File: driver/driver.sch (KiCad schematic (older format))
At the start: 107 parts, among them J1 OUT_A, J2 OUT_B, J3 UART_DEBUG, J4 USB_B_Micro, J5 CH340E module, J6 1602 I2C LCD, J7 IN_VCC, J8 IN_GND, Q1 TPHR6503PL, Q2 TPHR6503PL, Q3 TPHR6503PL, Q4 TPHR6503PL, SW1 SW_Push, SW2 SW_Push, U1 MT3608, U10 PC817, U2 AMS1117-5.0, U3 AMS1117-3.3, U4 TC4427, U5 TC4427, U6 STM32F103C8Tx, U7 INA226, U8 MCP9804_MSOP, U9 PC817, Y1 8MHz

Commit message: driver: Continue layout
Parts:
- removed C6: 100u, Capacitor_THT:CP_Radial_D12.5mm_P5.00mm, symbol Device:CP_Small
- removed C7, C8: 1u, Capacitors_SMD:C_0603_HandSoldering, symbol Device:C_Small
- removed R6: 10R .5W, Resistor_SMD:R_1206_3216Metric_Pad1.42x1.75mm_HandSolder, symbol Device:R_Small
- added C6: 100n, Capacitors_SMD:C_0603_HandSoldering, symbol Device:C_Small
- C15: footprint Capacitors_SMD:C_0603_HandSoldering -> Capacitor_THT:CP_Radial_D10.0mm_P5.00mm
- C19, C2, C3: footprint Capacitor_THT:CP_Radial_D12.5mm_P5.00mm -> Capacitor_THT:CP_Radial_D10.0mm_P5.00mm
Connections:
- net +3V3: now also C6.1
- net GND: now also C6.2; no longer U8.4 (GND), U8.5 (A2), U8.6 (A1), U8.7 (A0)
- net GND_MEAS: now also U8.4 (GND), U8.5 (A2), U8.6 (A1), U8.7 (A0)
- net LED2: now also U6.15 (PA5); no longer U6.20 (PB2)
- net LED5: now also U6.16 (PA6); no longer U6.15 (PA5)
- net LED6: now also U6.20 (PB2); no longer U6.16 (PA6)
- net at C15.1, C16.1, R7.2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: now also U2.3 (VI)
- net at D4.2 (A): now also R16.2; no longer R13.2
- net at D7.2 (A): now also R13.2; no longer R16.2
- net at D8.2 (A): now also R18.2; no longer R17.2
- net at D9.2 (A): now also R17.2; no longer R18.2
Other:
- moved on the sheet: C29, D4, D7, D8, D9
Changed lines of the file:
@@
 F 0 "C15" H 13000 4300 50  0000 L CNN
 F 1 "100u" H 13000 4200 50  0000 L CNN
-F 2 "Capacitors_SMD:C_0603_HandSoldering" H 13250 4250 50  0001 C CNN
+F 2 "Capacitor_THT:CP_Radial_D10.0mm_P5.00mm" H 13250 4250 50  0001 C CNN
 F 3 "~" H 13250 4250 50  0001 C CNN
 	1    13250 4250
@@
 $EndComp
 Wire Wire Line
-	12950 4100 13250 4100
-Wire Wire Line
 	13250 4100 13250 4150
 Wire Wire Line
@@
 F 0 "C19" H 15200 4300 50  0000 L CNN
 F 1 "470u" H 15200 4200 50  0000 L CNN
-F 2 "Capacitor_THT:CP_Radial_D12.5mm_P5.00mm" H 15100 4250 50  0001 C CNN
+F 2 "Capacitor_THT:CP_Radial_D10.0mm_P5.00mm" H 15100 4250 50  0001 C CNN
 F 3 "~" H 15100 4250 50  0001 C CNN
 	1    15100 4250
@@
 	13600 2200 13600 2050
 Connection ~ 13600 2050
-Wire Wire Line
-	12650 2050 12650 3200
 Connection ~ 12650 4100
 Wire Wire Line
@@
 F 0 "C2" H 15700 2150 50  0000 L CNN
 F 1 "470u" H 15700 2050 50  0000 L CNN
-F 2 "Capacitor_THT:CP_Radial_D12.5mm_P5.00mm" H 15600 2100 50  0001 C CNN
+F 2 "Capacitor_THT:CP_Radial_D10.0mm_P5.00mm" H 15600 2100 50  0001 C CNN
 F 3 "~" H 15600 2100 50  0001 C CNN
 	1    15600 2100
@@
 F 0 "C3" H 12850 2300 50  0000 L CNN
 F 1 "470u" H 12850 2200 50  0000 L CNN
-F 2 "Capacitor_THT:CP_Radial_D12.5mm_P5.00mm" H 13100 2250 50  0001 C CNN
+F 2 "Capacitor_THT:CP_Radial_D10.0mm_P5.00mm" H 13100 2250 50  0001 C CNN
 F 3 "~" H 13100 2250 50  0001 C CNN
 	1    13100 2250
@@
 L Device:C_Small C29
 U 1 1 5C5F270F
-P 11600 7750
-F 0 "C29" H 11692 7796 50  0000 L CNN
-F 1 "100n" H 11700 7700 50  0000 L CNN
-F 2 "Capacitors_SMD:C_0603_HandSoldering" H 11600 7750 50  0001 C CNN
-F 3 "~" H 11600 7750 50  0001 C CNN
-	1    11600 7750
+P 11450 7750
+F 0 "C29" H 11542 7796 50  0000 L CNN
+F 1 "100n" H 11550 7700 50  0000 L CNN
+F 2 "Capacitors_SMD:C_0603_HandSoldering" H 11450 7750 50  0001 C CNN
+F 3 "~" H 11450 7750 50  0001 C CNN
+	1    11450 7750
 	1    0    0    -1
 $EndComp
@@
 L power:GND #PWR0119
 U 1 1 5C5F5707
-P 11600 7850
-F 0 "#PWR0119" H 11600 7600 50  0001 C CNN
-F 1 "GND" H 11605 7677 50  0000 C CNN
-F 2 "" H 11600 7850 50  0001 C CNN
-F 3 "" H 11600 7850 50  0001 C CNN
-	1    11600 7850
+P 11450 7850
+F 0 "#PWR0119" H 11450 7600 50  0001 C CNN
+F 1 "GND" H 11455 7677 50  0000 C CNN
+F 2 "" H 11450 7850 50  0001 C CNN
+F 3 "" H 11450 7850 50  0001 C CNN
+	1    11450 7850
 	1    0    0    -1
 $EndComp
@@
 L power:+3V3 #PWR0128
 U 1 1 5C7621FB
-P 11600 7650
-F 0 "#PWR0128" H 11600 7500 50  0001 C CNN
-F 1 "+3V3" H 11615 7823 50  0000 C CNN
-F 2 "" H 11600 7650 50  0001 C CNN
-F 3 "" H 11600 7650 50  0001 C CNN
-	1    11600 7650
+P 11450 7650
+F 0 "#PWR0128" H 11450 7500 50  0001 C CNN
+F 1 "+3V3" H 11465 7823 50  0000 C CNN
+F 2 "" H 11450 7650 50  0001 C CNN
+F 3 "" H 11450 7650 50  0001 C CNN
+	1    11450 7650
 	1    0    0    -1
 $EndComp
@@
 $EndComp
 $Comp
-L Device:C_Small C8
-U 1 1 5D0CB164
-P 14400 3350
-F 0 "C8" H 14492 3396 50  0000 L CNN
-F 1 "1u" H 14500 3300 50  0000 L CNN
-F 2 "Capacitors_SMD:C_0603_HandSoldering" H 14400 3350 50  0001 C CNN
-F 3 "~" H 14400 3350 50  0001 C CNN
-	1    14400 3350
-	1    0    0    -1
-$EndComp
-Wire Wire Line
-	14400 3450 14400 3500
-Wire Wire Line
-	14400 3250 14400 3200
-Wire Wire Line
-	14400 3200 14300 3200
-$Comp
-L Device:C_Small C7
-U 1 1 5D0CB16E
-P 13600 3350
-F 0 "C7" H 13400 3400 50  0000 L CNN
-F 1 "1u" H 13400 3300 50  0000 L CNN
-F 2 "Capacitors_SMD:C_0603_HandSoldering" H 13600 3350 50  0001 C CNN
-F 3 "~" H 13600 3350 50  0001 C CNN
-	1    13600 3350
-	1    0    0    -1
-$EndComp
-Wire Wire Line
-	13600 3500 13600 3450
-Wire Wire Line
-	13600 3250 13600 3200
-Wire Wire Line
-	13600 3200 13700 3200
-$Comp
-L Device:CP_Small C6
-U 1 1 5D0CB178
-P 13250 3350
-F 0 "C6" H 13000 3400 50  0000 L CNN
-F 1 "100u" H 13000 3300 50  0000 L CNN
-F 2 "Capacitor_THT:CP_Radial_D12.5mm_P5.00mm" H 13250 3350 50  0001 C CNN
-F 3 "~" H 13250 3350 50  0001 C CNN
-	1    13250 3350
-	1    0    0    -1
-$EndComp
-$Comp
-L Device:R_Small R6
-U 1 1 5D0CB17F
-P 12850 3200
-F 0 "R6" V 12654 3200 50  0000 C CNN
-F 1 "10R .5W" V 12745 3200 50  0000 C CNN
-F 2 "Resistor_SMD:R_1206_3216Metric_Pad1.42x1.75mm_HandSolder" H 12850 3200 50  0001 C CNN
-F 3 "~" H 12850 3200 50  0001 C CNN
-	1    12850 3200
-	0    -1   1    0
-$EndComp
-Wire Wire Line
-	12950 3200 13250 3200
-Wire Wire Line
-	13250 3200 13250 3250
-Wire Wire Line
-	13250 3200 13600 3200
-Connection ~ 13250 3200
-Connection ~ 13600 3200
-$Comp
 L power:GND #PWR0140
 U 1 1 5D0CB18B
@@
 	1    0    0    -1
 $EndComp
-Wire Wire Line
-	14400 3500 14000 3500
-Wire Wire Line
-	13250 3500 13250 3450
-Connection ~ 13600 3500
-Wire Wire Line
-	13600 3500 13250 3500
 Connection ~ 14000 3500
-Wire Wire Line
-	14000 3500 13600 3500
 Wire Wire Line
 	14000 3500 14000 3550
@@
 	14750 3250 14750 3200
 Wire Wire Line
-	14750 3200 14400 3200
-Connection ~ 14400 3200
-Wire Wire Line
-	14400 3500 14750 3500
-Wire Wire Line
 	14750 3500 14750 3450
-Connection ~ 14400 3500
 $Comp
 L Device:C_Small C9
@@
 Wire Wire Line
 	15100 3100 15100 3200
-Wire Wire Line
-	12750 3200 12650 3200
-Connection ~ 12650 3200
-Wire Wire Line
-	12650 3200 12650 4100
 $Comp
 L Device:LED_Small_ALT D2
@@
 L Device:LED_Small_ALT D4
 U 1 1 5D120495
-P 18100 5600
-F 0 "D4" V 18200 5550 50  0000 R CNN
-F 1 "cyan" V 18055 5532 50  0001 R CNN
-F 2 "LED_SMD:LED_PLCC_2835_Handsoldering" V 18100 5600 50  0001 C CNN
-F 3 "~" V 18100 5600 50  0001 C CNN
-	1    18100 5600
+P 18800 5600
+F 0 "D4" V 18900 5550 50  0000 R CNN
+F 1 "cyan" V 18755 5532 50  0001 R CNN
+F 2 "LED_SMD:LED_PLCC_2835_Handsoldering" V 18800 5600 50  0001 C CNN
+F 3 "~" V 18800 5600 50  0001 C CNN
+	1    18800 5600
 	0    -1   -1   0
 $EndComp
@@
 L Device:LED_Small_ALT D7
 U 1 1 5D12562A
-P 18800 5600
-F 0 "D7" V 18900 5550 50  0000 R CNN
-F 1 "pink" V 18755 5532 50  0001 R CNN
-F 2 "LED_SMD:LED_PLCC_2835_Handsoldering" V 18800 5600 50  0001 C CNN
-F 3 "~" V 18800 5600 50  0001 C CNN
-	1    18800 5600
+P 18100 5600
+F 0 "D7" V 18200 5550 50  0000 R CNN
+F 1 "pink" V 18055 5532 50  0001 R CNN
+F 2 "LED_SMD:LED_PLCC_2835_Handsoldering" V 18100 5600 50  0001 C CNN
+F 3 "~" V 18100 5600 50  0001 C CNN
+	1    18100 5600
 	0    -1   -1   0
 $EndComp
@@
 L Device:LED_Small_ALT D8
 U 1 1 5D1365C9
+P 19200 5600
+F 0 "D8" V 19300 5550 50  0000 R CNN
+F 1 "pink" V 19155 5532 50  0001 R CNN
+F 2 "LED_SMD:LED_PLCC_2835_Handsoldering" V 19200 5600 50  0001 C CNN
+F 3 "~" V 19200 5600 50  0001 C CNN
+	1    19200 5600
+	0    -1   -1   0
+$EndComp
+$Comp
+L Device:LED_Small_ALT D9
+U 1 1 5D138D62
 P 19000 5600
-F 0 "D8" V 19100 5550 50  0000 R CNN
+F 0 "D9" V 19100 5550 50  0000 R CNN
 F 1 "pink" V 18955 5532 50  0001 R CNN
 F 2 "LED_SMD:LED_PLCC_2835_Handsoldering" V 19000 5600 50  0001 C CNN
 F 3 "~" V 19000 5600 50  0001 C CNN
 	1    19000 5600
-	0    -1   -1   0
-$EndComp
-$Comp
-L Device:LED_Small_ALT D9
-U 1 1 5D138D62
-P 19200 5600
-F 0 "D9" V 19300 5550 50  0000 R CNN
-F 1 "pink" V 19155 5532 50  0001 R CNN
-F 2 "LED_SMD:LED_PLCC_2835_Handsoldering" V 19200 5600 50  0001 C CNN
-F 3 "~" V 19200 5600 50  0001 C CNN
-	1    19200 5600
 	0    -1   -1   0
 $EndComp
@@
 Text Label 15550 6300 0    50   ~ 0
 LED1
-Text Label 15550 6400 0    50   ~ 0
+Text Label 17850 6700 2    50   ~ 0
 LED2
 Text Label 17850 6500 2    50   ~ 0
@@
 Text Label 17850 6600 2    50   ~ 0
 LED4
-Text Label 17850 6700 2    50   ~ 0
+Text Label 17850 6800 2    50   ~ 0
 LED5
-Text Label 17850 6800 2    50   ~ 0
+Text Label 15550 6400 0    50   ~ 0
 LED6
 Text Label 17850 6900 2    50   ~ 0
@@
 Wire Wire Line
 	12800 8050 13150 8050
-Wire Wire Line
-	13050 8850 13050 8650
 Wire Wire Line
 	13050 8450 13150 8450
@@
 Text Label 9000 4100 0    50   ~ 0
 VIN
-$Comp
-L power:GND #PWR0145
-U 1 1 5D8E1654
-P 13050 8850
-F 0 "#PWR0145" H 13050 8600 50  0001 C CNN
-F 1 "GND" H 13055 8677 50  0000 C CNN
-F 2 "" H 13050 8850 50  0001 C CNN
-F 3 "" H 13050 8850 50  0001 C CNN
-	1    13050 8850
-	1    0    0    -1
-$EndComp
-$Comp
-L power:GND #PWR0144
-U 1 1 5D8E115C
-P 13550 8850
-F 0 "#PWR0144" H 13550 8600 50  0001 C CNN
-F 1 "GND" H 13555 8677 50  0000 C CNN
-F 2 "" H 13550 8850 50  0001 C CNN
-F 3 "" H 13550 8850 50  0001 C CNN
-	1    13550 8850
-	1    0    0    -1
-$EndComp
+Wire Wire Line
+	12650 2050 12650 4100
+Wire Wire Line
+	12950 4100 13250 4100
+Wire Wire Line
+	13250 3200 13250 4100
+Wire Wire Line
+	13250 3200 13700 3200
+Wire Wire Line
+	14300 3200 14750 3200
+Wire Wire Line
+	14000 3500 14750 3500
+$Comp
+L Device:C_Small C6
+U 1 1 5C95D870
+P 11800 7750
+F 0 "C6" H 11892 7796 50  0000 L CNN
+F 1 "100n" H 11900 7700 50  0000 L CNN
+F 2 "Capacitors_SMD:C_0603_HandSoldering" H 11800 7750 50  0001 C CNN
+F 3 "~" H 11800 7750 50  0001 C CNN
+	1    11800 7750
+	1    0    0    -1
+$EndComp
+$Comp
+L power:GND #PWR0147
+U 1 1 5C95D877
+P 11800 7850
+F 0 "#PWR0147" H 11800 7600 50  0001 C CNN
+F 1 "GND" H 11805 7677 50  0000 C CNN
+F 2 "" H 11800 7850 50  0001 C CNN
+F 3 "" H 11800 7850 50  0001 C CNN
+	1    11800 7850
+	1    0    0    -1
+$EndComp
+$Comp
+L power:+3V3 #PWR0148
+U 1 1 5C95D87D
+P 11800 7650
+F 0 "#PWR0148" H 11800 7500 50  0001 C CNN
+F 1 "+3V3" H 11815 7823 50  0000 C CNN
+F 2 "" H 11800 7650 50  0001 C CNN
+F 3 "" H 11800 7650 50  0001 C CNN
+	1    11800 7650
+	1    0    0    -1
+$EndComp
+Text Label 12400 8900 0    50   ~ 0
+GND_MEAS
+Wire Wire Line
+	13550 8850 13550 8900
+Wire Wire Line
+	13550 8900 13050 8900
+Wire Wire Line
+	13050 8650 13050 8900
+Connection ~ 13050 8900
+Wire Wire Line
+	13050 8900 12400 8900
 $EndSCHEMATC

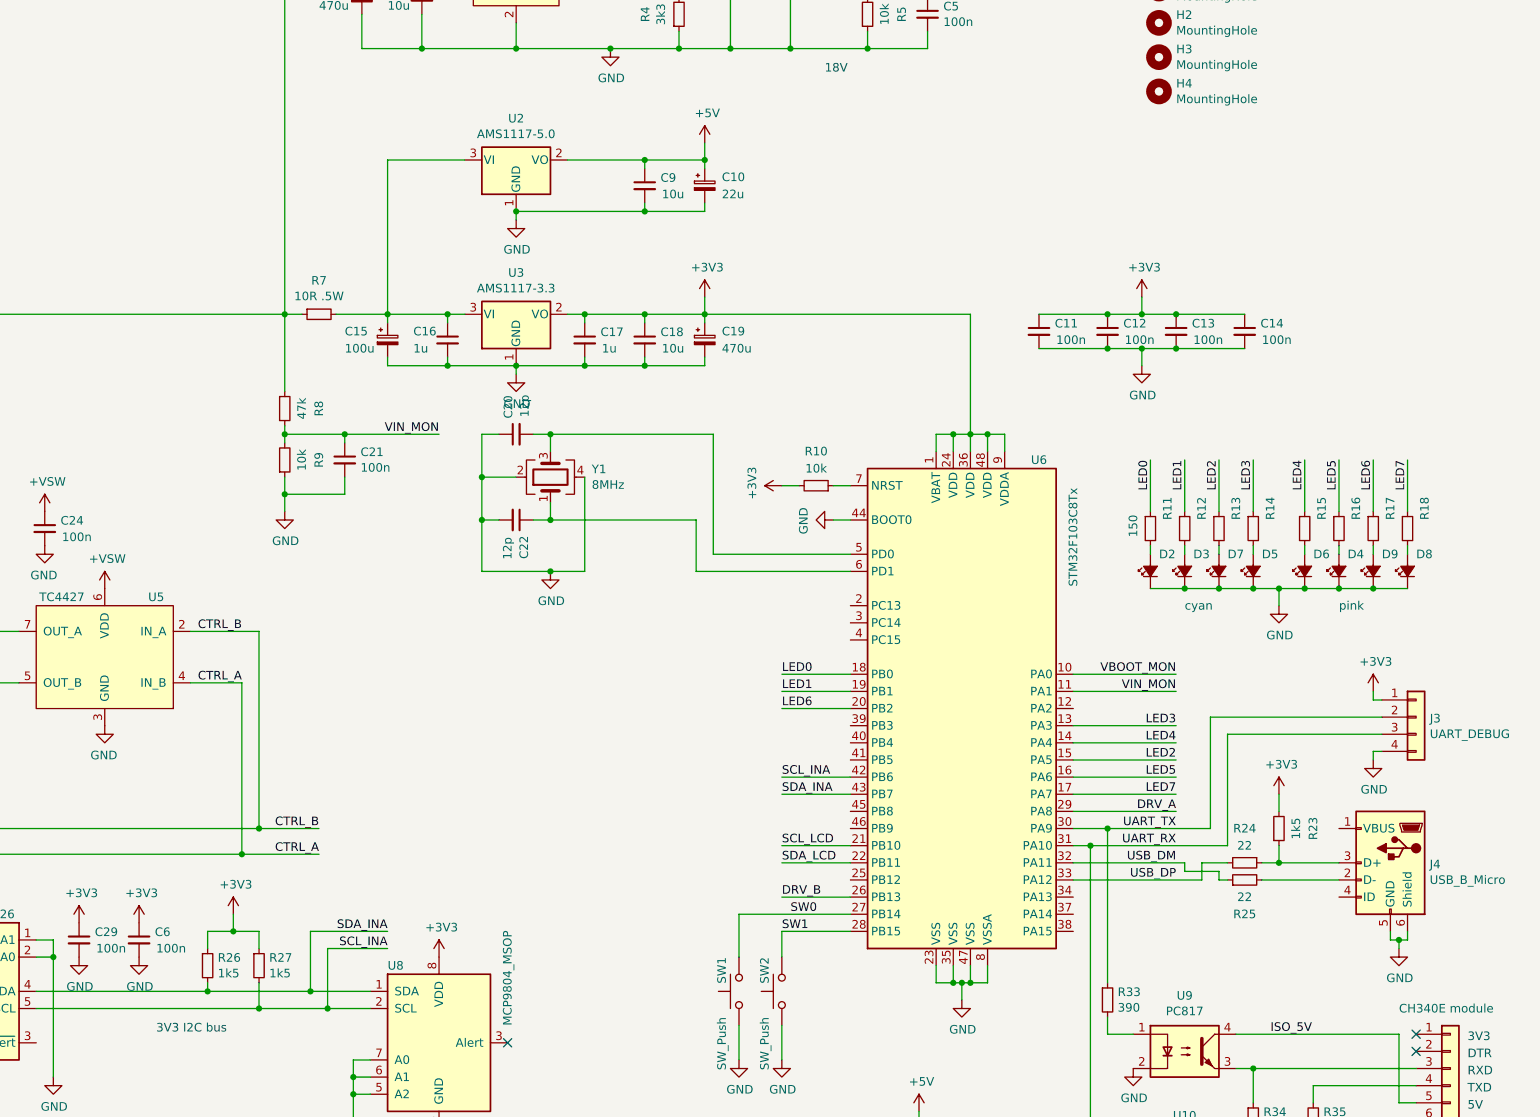
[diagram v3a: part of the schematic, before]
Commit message: driver: Initial layout almost done
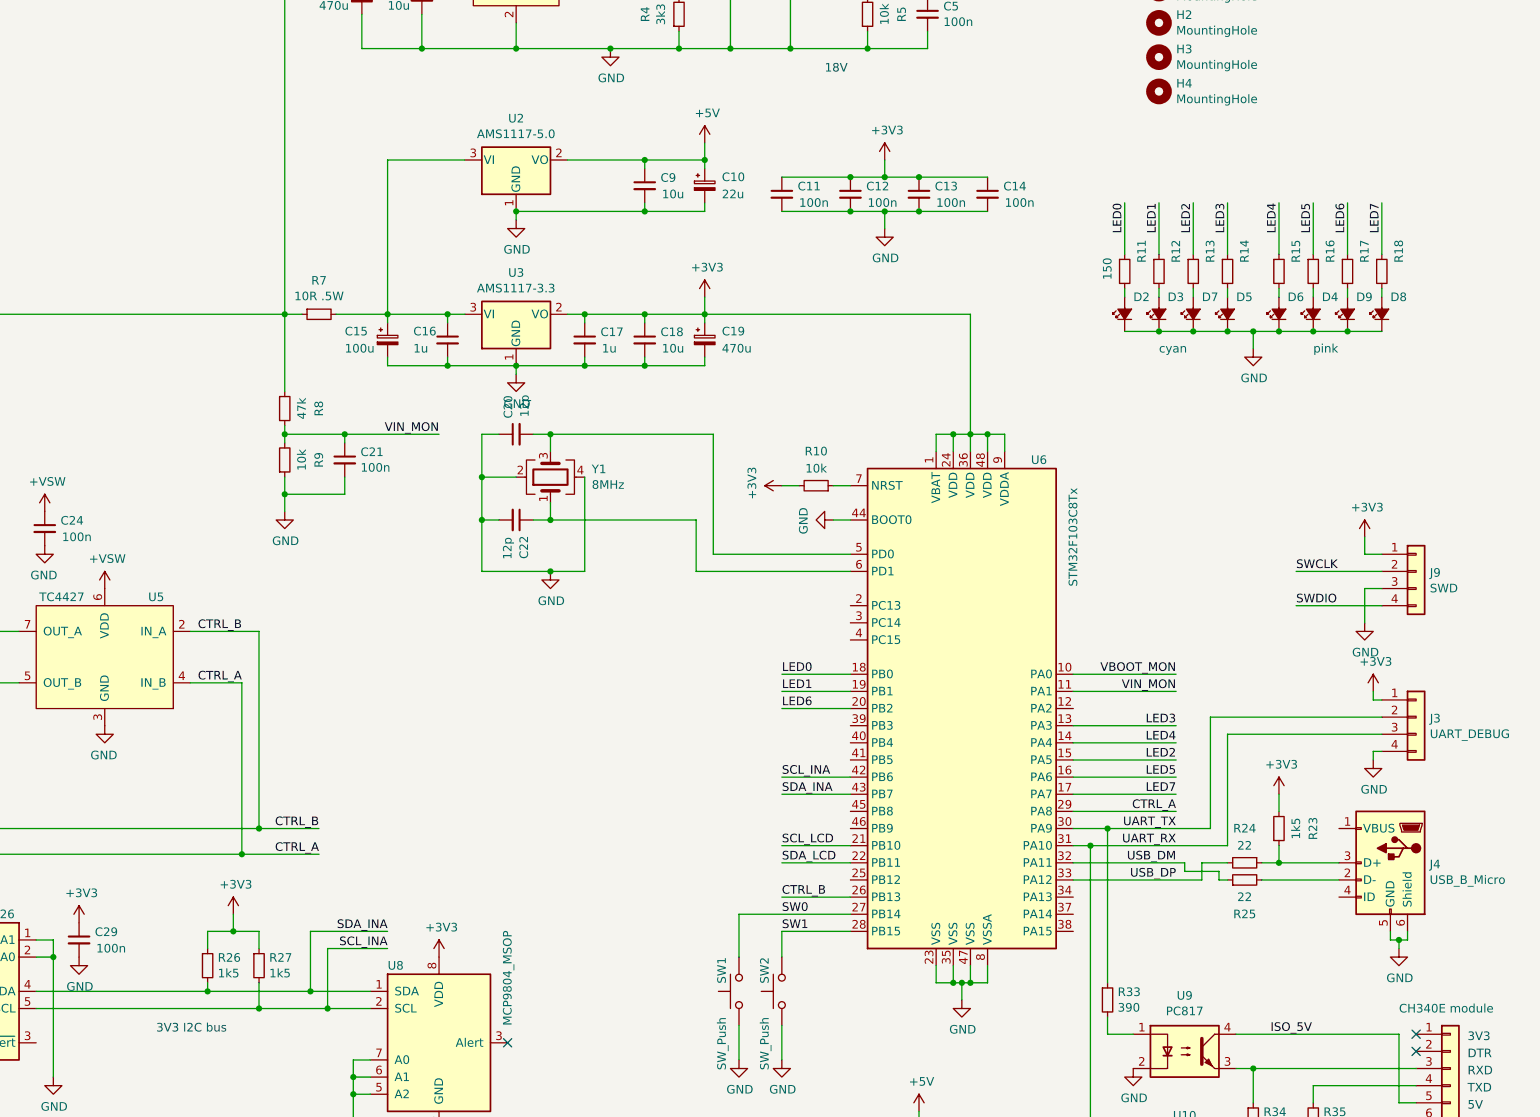
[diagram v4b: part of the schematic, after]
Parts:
- removed C6: 100n, Capacitors_SMD:C_0603_HandSoldering, symbol Device:C_Small
- added J9: SWD, Pin_Headers:Pin_Header_Straight_1x04_Pitch2.54mm, symbol Connector_Generic:Conn_01x04
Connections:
- net DRV_A is gone; now on net CTRL_A: U6.29 (PA8)
- net DRV_B is gone; now on net CTRL_B: U6.26 (PB13)
- net +3V3: now also J9.1 (Pin_1)
- net GND: now also J9.3 (Pin_3)
- new net SWCLK: J9.2 (Pin_2)
- new net SWDIO: J9.4 (Pin_4)
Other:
- moved on the sheet: C11, C12, C13, C14, D2, D3, D4, D5, D6, D7, D8, D9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

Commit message: driver: Finish initial routing
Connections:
- net LED0: now also U6.3 (PC14); no longer U6.18 (PB0)
- net LED6: now also U6.2 (PC13); no longer U6.20 (PB2)
- net SWCLK: now also U6.37 (PA14)
- net SWDIO: now also U6.34 (PA13)
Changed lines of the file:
@@
 Wire Wire Line
 	17550 3450 17550 3750
-Text Label 15550 6200 0    50   ~ 0
+Text Label 15550 5900 0    50   ~ 0
 LED0
 Text Label 15550 6300 0    50   ~ 0
@@
 Text Label 17850 6800 2    50   ~ 0
 LED5
-Text Label 15550 6400 0    50   ~ 0
+Text Label 15550 5800 0    50   ~ 0
 LED6
 Text Label 17850 6900 2    50   ~ 0
@@
 	17250 6600 17850 6600
 Wire Wire Line
-	17850 6500 17250 6500
-Wire Wire Line
-	15550 6200 15950 6200
-Wire Wire Line
 	15950 6300 15550 6300
-Wire Wire Line
-	15550 6400 15950 6400
 $Comp
 L Switch:SW_Push SW1
@@
 Text Label 18550 5600 0    50   ~ 0
 SWCLK
+Wire Wire Line
+	17850 6500 17250 6500
+Wire Wire Line
+	15550 5800 15950 5800
+Wire Wire Line
+	15550 5900 15950 5900
+Text Label 17850 7600 2    50   ~ 0
+SWCLK
+Text Label 17850 7500 2    50   ~ 0
+SWDIO
+Wire Wire Line
+	17250 7500 17850 7500
+Wire Wire Line
+	17850 7600 17250 7600
 $EndSCHEMATC

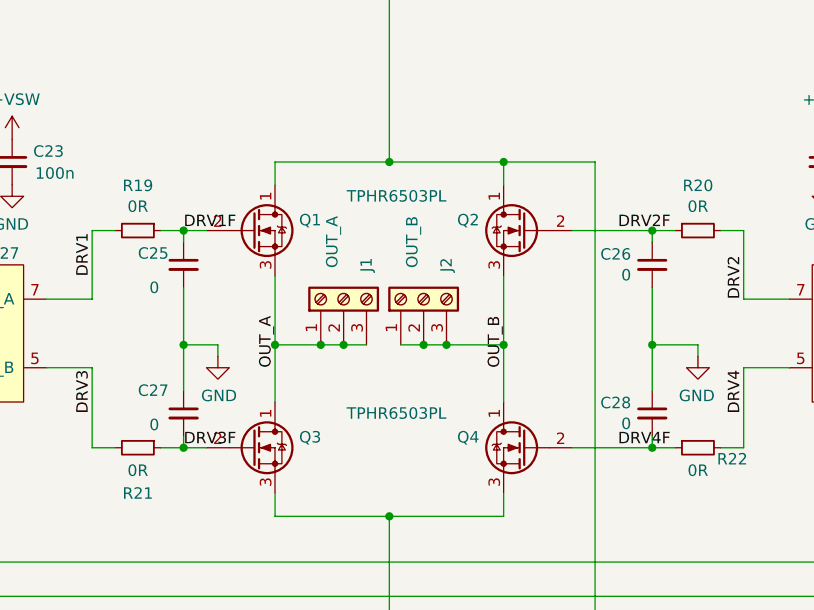
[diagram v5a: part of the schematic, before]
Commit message: driver: Fixup SWD header, swap driver outputs for VSW split, finish silk
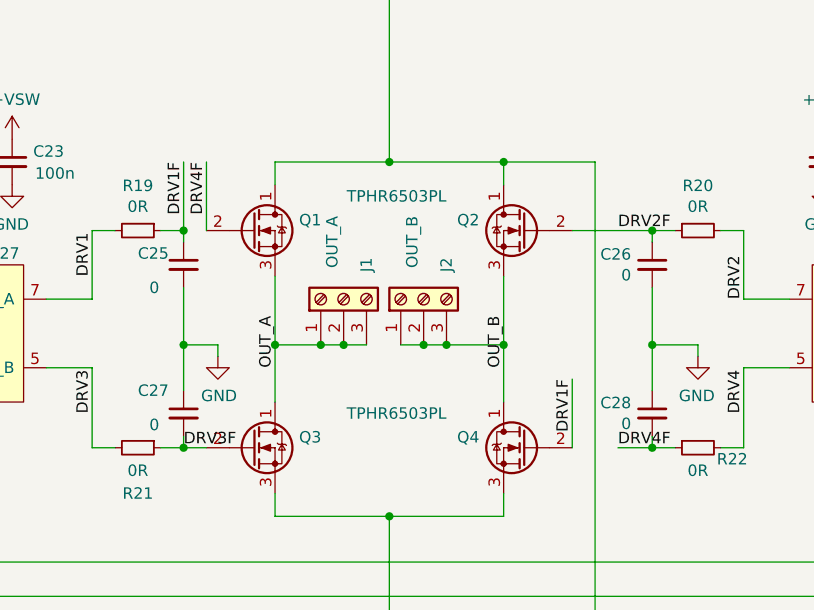
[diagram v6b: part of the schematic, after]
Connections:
- net DRV1F: now also Q4.2 (G); no longer Q1.2 (G)
- net DRV4F: now also Q1.2 (G); no longer Q4.2 (G)
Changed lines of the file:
@@
 Wire Wire Line
 	8450 5700 8450 5650
-Wire Wire Line
-	8450 5650 8550 5650
 $Comp
 L power:GND #PWR0103
@@
 Wire Wire Line
 	9350 8500 6200 8500
-Connection ~ 8450 5650
 $Comp
 L Device:R_Small R21
@@
 	10150 5650 10500 5650
 Wire Wire Line
-	10150 6600 10500 6600
-Wire Wire Line
 	10500 6550 10500 6600
-Connection ~ 10500 6600
 Wire Wire Line
 	10500 6600 10600 6600
@@
 Text Label 8050 5850 1    50   ~ 0
 DRV1
-Text Label 8450 5650 0    50   ~ 0
+Text Label 8450 5350 3    50   ~ 0
 DRV1F
 Text Label 8450 6600 0    50   ~ 0
@@
 Wire Wire Line
 	17850 7600 17250 7600
+Wire Wire Line
+	10350 6600 10500 6600
+Connection ~ 10500 6600
+Text Label 8550 5350 3    50   ~ 0
+DRV4F
+Wire Wire Line
+	8550 5350 8550 5650
+Wire Wire Line
+	8450 5350 8450 5650
+Connection ~ 8450 5650
+Text Label 10150 6300 3    50   ~ 0
+DRV1F
+Wire Wire Line
+	10150 6300 10150 6600
 $EndSCHEMATC
